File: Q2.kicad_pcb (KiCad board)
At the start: 2 copper layers, 87.7 x 51.6 mm, 145 parts, among them U1 LM317, U10 SP-2U1+, U11 SMA, U12 LT1009, U13 TL974, U2 Teensy3.2, U3 SMA, U4 ROS-2536C-119+, U5 PMA4-33GLN+, U6 PGA-103+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

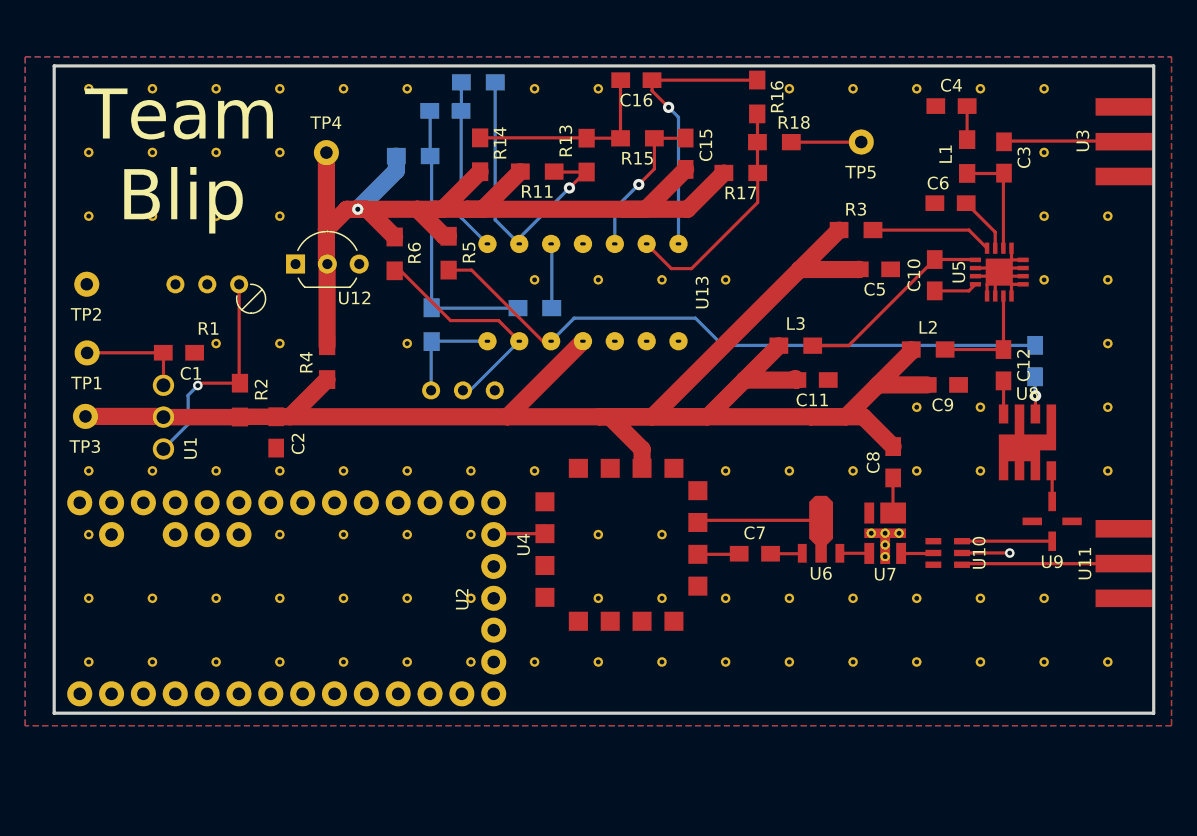
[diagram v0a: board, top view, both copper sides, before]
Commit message: PCB Fix + DFM Report + PCB Width Calculation
Fixed Track Width
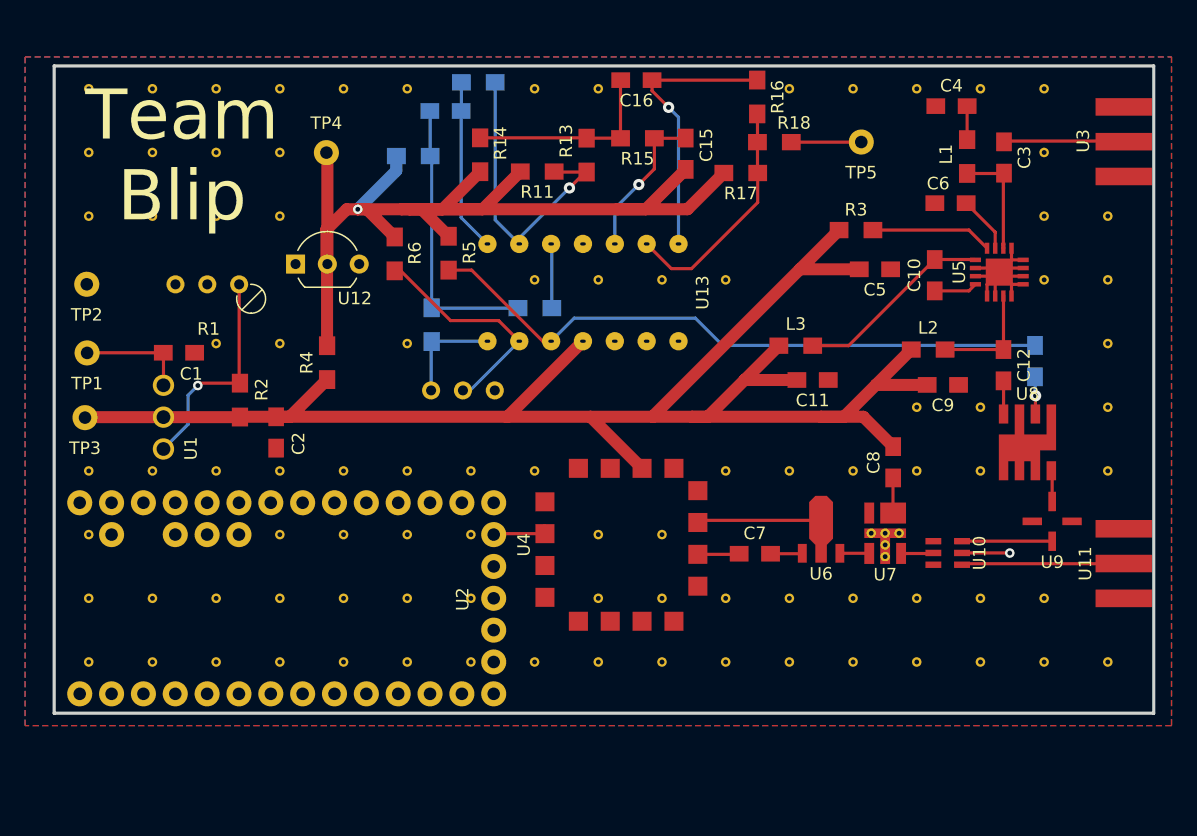
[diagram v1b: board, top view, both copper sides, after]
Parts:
- moved TP3 0.10 mm to (37.8, 59.2)
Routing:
- net /+5V: track 149.9 -> 137.9 mm
- net /+2.5V: track 78.8 -> 87.9 mm

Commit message: Update
Fix Ground Connection Issues
Cleaned Up Ground Connection
Fixed Via Ground Connection Issues
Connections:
- REF** pad 1: (no net) -> GND (x90)
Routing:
- net GND: track 40.6 -> 42.5 mm
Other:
- net class Default: trace_width 0.254 -> 0.508

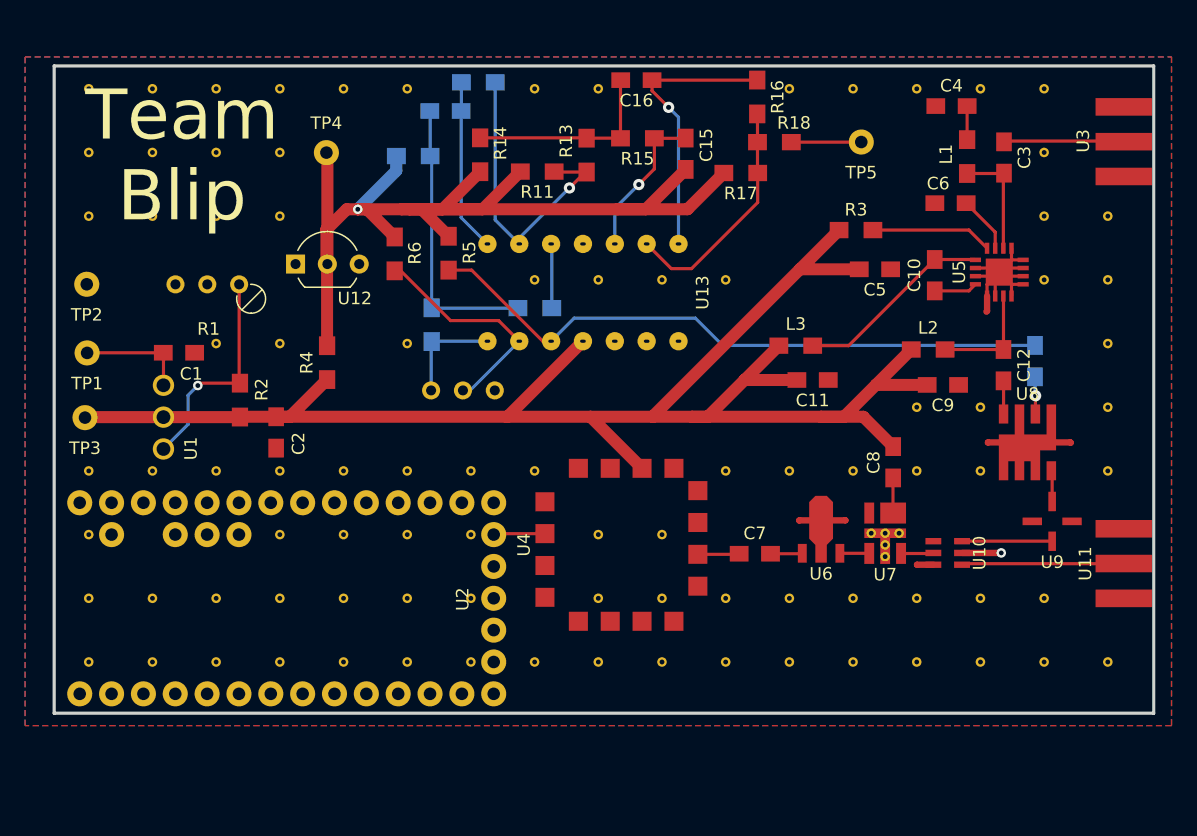
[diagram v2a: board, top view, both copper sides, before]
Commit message: Update
Fixed Missing LNA
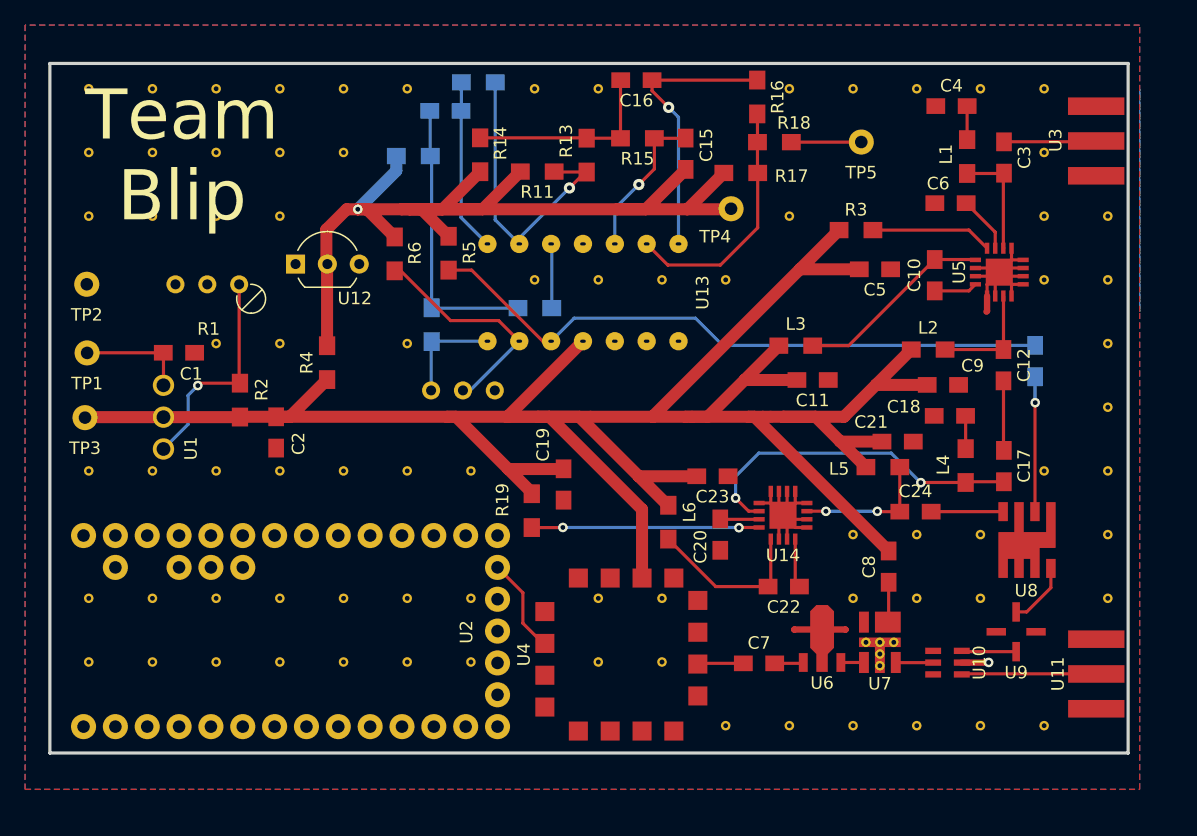
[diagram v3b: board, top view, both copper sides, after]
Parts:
- removed the REF** at (114.3, 73.7)
- removed the REF** at (114.3, 78.7)
- removed the REF** at (119.4, 78.7)
- removed the REF** at (99.1, 78.7)
- removed the REF** at (109.2, 63.5)
- removed the REF** at (109.2, 58.4)
- removed the REF** at (104.1, 63.5)
- removed the REF** at (104.1, 58.4)
- removed the REF** at (99.1, 63.5)
- removed the REF** at (94.0, 63.5)
- removed the REF** at (88.9, 63.5)
- removed the REF** at (88.9, 73.7)
- removed the REF** at (104.1, 78.7)
- removed the REF** at (83.8, 68.6)
- removed the REF** at (78.7, 68.6)
- removed the REF** at (73.7, 78.7)
- removed the REF** at (68.6, 68.6)
- removed the REF** at (63.5, 68.6)
- removed the REF** at (58.4, 68.6)
- removed the REF** at (53.3, 68.6)
- removed the REF** at (94.0, 78.7)
- removed the REF** at (88.9, 78.7)
- removed the REF** at (38.1, 68.6)
- removed the REF** at (73.7, 63.5)
- removed the REF** at (109.2, 78.7)
- removed the REF** at (94.0, 73.7)
- added C17: 56p, Q2Footprint:C_0805_HandSoldering, F.Cu at (111.1, 63.1)
- added C18: 0.1u, Q2Footprint:C_0805_HandSoldering, F.Cu at (106.8, 59.1)
- added C19: 0.1u, Q2Footprint:C_0805_HandSoldering, F.Cu at (76.0, 64.6)
- added C20: 1n, Q2Footprint:C_0805_HandSoldering, F.Cu at (88.5, 68.6)
- added C21: 0.1u, Q2Footprint:C_0805_HandSoldering, F.Cu at (102.6, 61.2)
- added C22: 82p, Q2Footprint:C_0805_HandSoldering, F.Cu at (93.5, 72.7)
- added C23: 0.1u, Q2Footprint:C_0805_HandSoldering, F.Cu at (87.8, 63.9)
- added C24: 0.1u, Q2Footprint:C_0805_HandSoldering, F.Cu at (104.0, 66.8)
- added L4: 15n, Q2Footprint:L_0805_HandSoldering, F.Cu at (108.0, 63.1)
- added L5: 82n, Q2Footprint:L_0805_HandSoldering, F.Cu at (101.4, 63.2)
- added L6: 5.6n, Q2Footprint:L_0805_HandSoldering, F.Cu at (84.3, 67.6)
- added R19: 1k, Q2Footprint:R_0805_HandSoldering, F.Cu at (73.4, 66.7)
- added REF**: via-15mil, Q2Footprint:via-15mil, F.Cu at (58.4, 38.1)
- added REF**: via-15mil, Q2Footprint:via-15mil, F.Cu at (114.3, 63.5)
- added REF**: via-15mil, Q2Footprint:via-15mil, F.Cu at (88.9, 83.8)
- added REF**: via-15mil, Q2Footprint:via-15mil, F.Cu at (94.0, 83.8)
- added REF**: via-15mil, Q2Footprint:via-15mil, F.Cu at (99.1, 83.8)
- added REF**: via-15mil, Q2Footprint:via-15mil, F.Cu at (99.1, 68.6)
- added REF**: via-15mil, Q2Footprint:via-15mil, F.Cu at (104.1, 83.8)
- added REF**: via-15mil, Q2Footprint:via-15mil, F.Cu at (109.2, 83.8)
- added REF**: via-15mil, Q2Footprint:via-15mil, F.Cu at (114.3, 83.8)
- added REF**: via-15mil, Q2Footprint:via-15mil, F.Cu at (119.4, 73.7)
- added REF**: via-15mil, Q2Footprint:via-15mil, F.Cu at (119.4, 68.6)
- added REF**: via-15mil, Q2Footprint:via-15mil, F.Cu at (94.0, 43.2)
- added REF**: via-15mil, Q2Footprint:via-15mil, F.Cu at (109.2, 68.6)
- added REF**: via-15mil, Q2Footprint:via-15mil, F.Cu at (104.1, 68.6)
- added U14: PMA4-33GLN+, Q2Footprint:PMA4-33GLN+, F.Cu at (93.5, 67.0)
- moved TP4 32.6 mm to (89.3, 42.6)
- moved U9 9.26 mm to (112.1, 76.3)
- moved U11 9.07 mm to (116.2, 79.7)
- moved U4 8.75 mm to (80.6, 78.1)
- moved C7 8.75 mm to (91.6, 78.8)
- moved U10 8.75 mm to (106.6, 78.8)
- moved U7 8.71 mm to (101.2, 77.2)
- moved U6 8.71 mm to (96.6, 76.9)
- moved C8 8.33 mm to (101.9, 71.1)
- moved U8 7.79 mm to (112.9, 69.0)
- moved U2 2.63 mm to (72.0, 76.3)
- moved U3 2.20 mm to (120.7, 37.2)
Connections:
- U8 pad 4: Net-(C12-Pad1) -> Net-(C24-Pad1)
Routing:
- net /+5V: track 137.9 -> 203.9 mm
- net Net-(C17-Pad1): track 0.00 -> 27.2 mm, vias 0 -> 2
- net Net-(R19-Pad1): track 0.00 -> 18.2 mm, vias 0 -> 2
- net Net-(C22-Pad1): track 0.00 -> 13.4 mm
- net Net-(C24-Pad2): track 0.00 -> 11.0 mm, vias 0 -> 2
- net Net-(C13-Pad2): track 2.99 -> 10.8 mm
- net GND: track 42.5 -> 50.1 mm
- net Net-(C24-Pad1): track 0.00 -> 5.81 mm
- net /+2.5V: track 87.9 -> 82.3 mm
- net Net-(C22-Pad2): track 0.00 -> 3.92 mm
- net Net-(U2-Pad18): track 4.23 -> 7.71 mm
- net Net-(C20-Pad1): track 0.00 -> 3.11 mm
- net Net-(C12-Pad1): track 2.64 -> 5.58 mm
- net Net-(U10-Pad3): track 7.19 -> 4.36 mm
- net Net-(U8-Pad8): track 2.48 -> 5.11 mm
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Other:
- board size 87.7 x 51.6 mm -> 86 x 55 mm
- net class Default: trace_width 0.508 -> 0.961

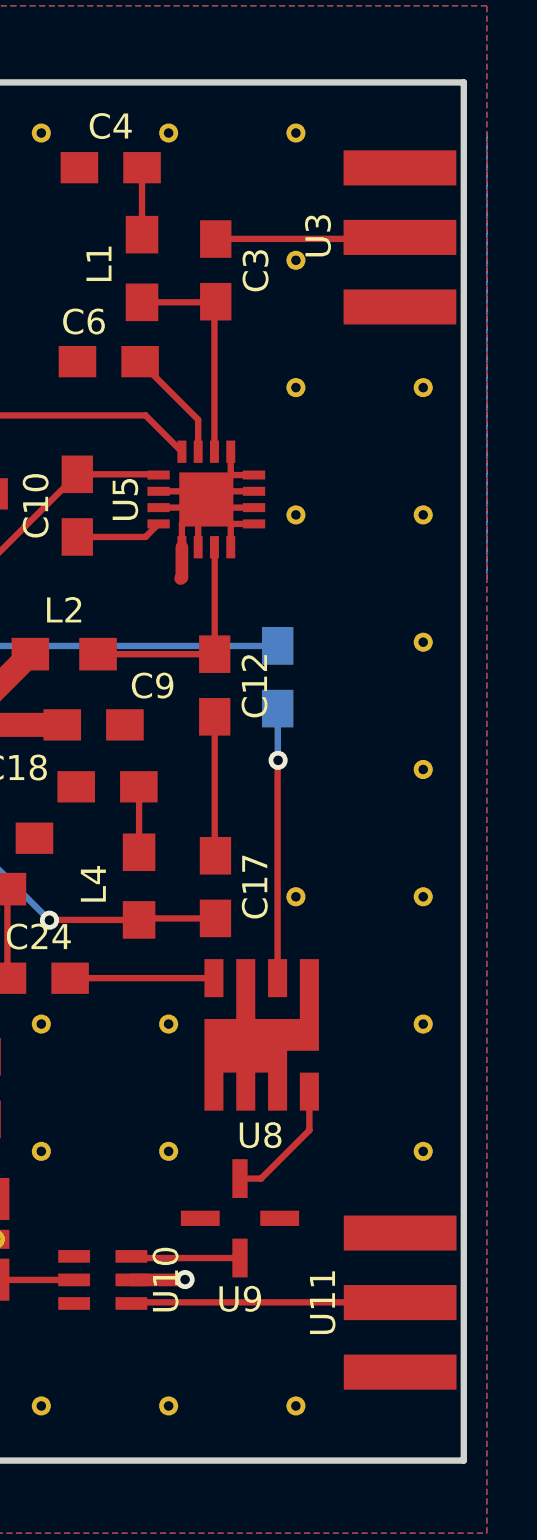
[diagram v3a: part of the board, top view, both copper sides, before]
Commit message: Update
Fixed SMA Edge
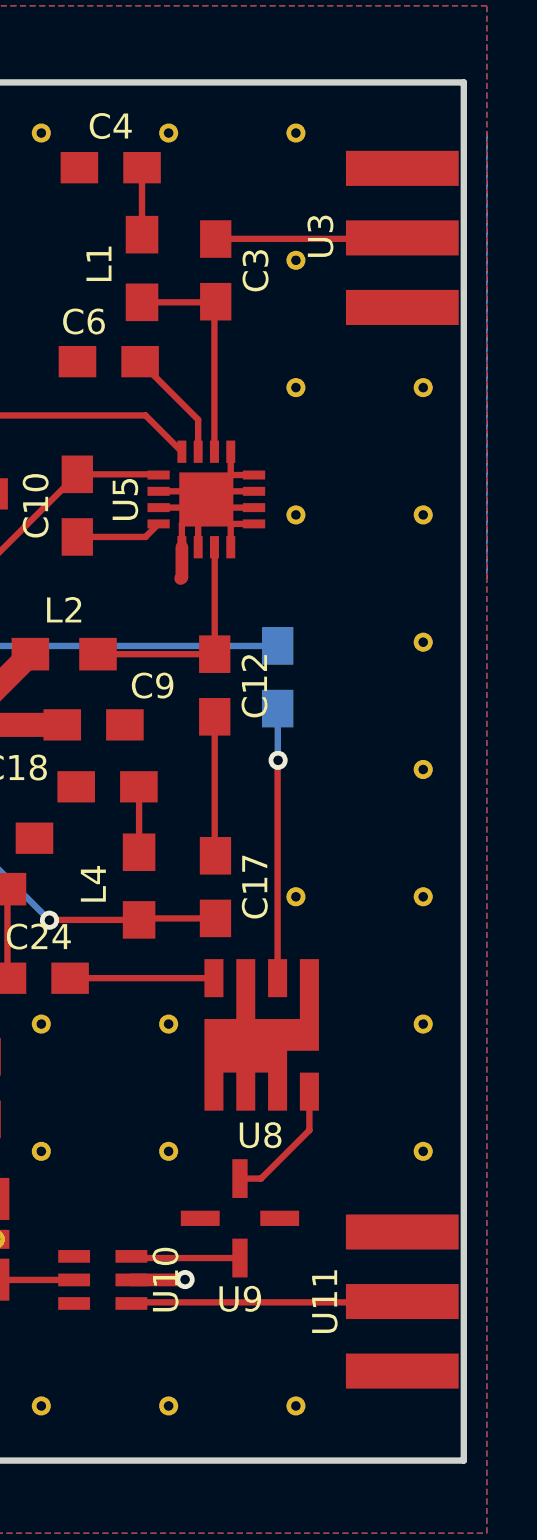
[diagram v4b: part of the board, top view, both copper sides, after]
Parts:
- moved U3 0.10 mm to (120.8, 37.2)
- moved U11 0.10 mm to (116.3, 79.7)
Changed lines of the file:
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@@
   )
   (module Q2Footprint:SMA (layer F.Cu)
-    (at 120.701 37.186 90)
+    (at 120.797 37.206 90)
     (fp_text reference U3 (at 0.061 -5.483 90) (layer F.SilkS)
       (effects (font (size 1 1) (thickness 0.15)))
@@
   )
   (module Q2Footprint:SMA (layer F.Cu)
-    (at 116.21 79.695 270)
+    (at 116.296 79.654 270)
     (fp_text reference U11 (at 0 0.8128 270) (layer F.SilkS)
       (effects (font (size 1 1) (thickness 0.15)))

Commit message: Update
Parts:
- C12, C24: value 0.1u -> 68p
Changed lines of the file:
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@@
     (links 240)
     (no_connects 0)
-    (area 34.872999 30.872999 121.127001 86.127001)
+    (area 33.02 27.94 122.5558 88.900001)
     (thickness 1.6)
     (drawings 5)
@@
       (effects (font (size 1 1) (thickness 0.15)))
     )
-    (fp_text value 0.1u (at 0 -1.524 90) (layer F.Fab)
+    (fp_text value 68p (at 0 -1.524 90) (layer F.Fab)
       (effects (font (size 1 1) (thickness 0.15)))
     )
@@
       (effects (font (size 1 1) (thickness 0.15)))
     )
-    (fp_text value 0.1u (at 0 -1.524 180) (layer F.Fab)
-      (effects (font (size 1 1) (thickness 0.15)))
-    )
+    (fp_text value 68p (at 0 -1.524 180) (layer F.Fab)
+      (effects (font (size 1 1) (thickness 0.15)))
+    )

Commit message: Update
Fixed LNA Connection
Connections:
- C20 pad 1: Net-(C20-Pad1) -> Net-(C18-Pad1)
- C6 pad 1: Net-(C6-Pad1) -> Net-(C4-Pad1)
- U14 pad 3: Net-(C20-Pad1) -> Net-(C18-Pad1)
- U5 pad 3: Net-(C6-Pad1) -> Net-(C4-Pad1)
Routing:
- net Net-(C18-Pad1): track 2.62 -> 31.1 mm, vias 0 -> 2
- net Net-(C4-Pad1): track 2.67 -> 14.3 mm
- net Net-(C6-Pad1): track 4.55 -> 0.00 mm
- net Net-(C20-Pad1): track 3.11 -> 0.00 mm
- net GND: track 50.1 -> 52.0 mm, vias 1 -> 2
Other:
- net class Default: trace_width 0.961 -> 0.508

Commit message: Update
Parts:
- added C25: 1n, Q2Footprint:C_0805_HandSoldering, B.Cu at (73.8, 34.8)
- added REF**: via-15mil, Q2Footprint:via-15mil, F.Cu at (88.9, 38.1)
- added REF**: via-15mil, Q2Footprint:via-15mil, F.Cu at (88.9, 33.0)
- added REF**: via-15mil, Q2Footprint:via-15mil, F.Cu at (94.0, 38.1)
- added REF**: via-15mil, Q2Footprint:via-15mil, F.Cu at (104.1, 43.2)
- added REF**: via-15mil, Q2Footprint:via-15mil, F.Cu at (104.1, 38.1)
- added REF**: via-15mil, Q2Footprint:via-15mil, F.Cu at (99.1, 38.1)
- R13: value 17.4 -> 17.4k
- moved R18 5.70 mm to (95.6, 32.3)
- moved TP5 2.91 mm to (97.0, 36.2)
- turned R16 to 270 degrees
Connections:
- R16 pad 1: Net-(R16-Pad1) -> Net-(C16-Pad2)
- R16 pad 2: Net-(C16-Pad2) -> Net-(R16-Pad2)
- R17 pad 2: Net-(R16-Pad1) -> Net-(R16-Pad2)
- R18 pad 2: Net-(R16-Pad1) -> Net-(C16-Pad2)
- U12 pad 1: Net-(U12-Pad1) -> GND
- U12 pad 3: GND -> Net-(U12-Pad3)
- U13 pad 9: Net-(R16-Pad1) -> Net-(R16-Pad2)
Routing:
- net Net-(R16-Pad2): track 0.00 -> 19.9 mm
- net Net-(R16-Pad1): track 19.9 -> 0.00 mm
- net Net-(C25-Pad2): track 5.14 -> 15.8 mm
- net /+2.5V: track 82.3 -> 87.1 mm, vias 1 -> 2
- net Net-(C16-Pad2): track 22.3 -> 25.2 mm
- net Net-(R18-Pad1): track 5.58 -> 3.88 mm
- net Net-(R10-Pad1): track 24.7 -> 24.1 mm
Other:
- net class Default: trace_width 0.508 -> 0.254
- rule trace_min: 0.254 -> 0.1524

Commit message: Update
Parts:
- added REF**: via-15mil, Q2Footprint:via-15mil, F.Cu at (99.1, 43.2)
- added REF**: via-15mil, Q2Footprint:via-15mil, F.Cu at (58.4, 43.2)
- added REF**: via-15mil, Q2Footprint:via-15mil, F.Cu at (43.2, 53.3)
- added REF**: via-15mil, Q2Footprint:via-15mil, F.Cu at (38.1, 48.3)
- added REF**: via-15mil, Q2Footprint:via-15mil, F.Cu at (88.9, 73.7)
- moved C1 11.6 mm to (45.3, 65.7)
- moved TP1 11.6 mm to (37.7, 65.7)
- moved L3 8.38 mm to (101.1, 48.3)
- moved C5 6.34 mm to (94.5, 48.5)
- moved C11 5.56 mm to (98.1, 51.2)
- moved C9 5.40 mm to (100.9, 57.7)
- moved TP2 4.75 mm to (37.9, 53.4)
- moved C23 4.40 mm to (83.4, 64.0)
- moved C19 3.82 mm to (72.5, 62.9), turned to 0 degrees
- moved C21 3.49 mm to (99.1, 61.0)
- moved L2 2.36 mm to (103.4, 55.5)
- moved R3 2.21 mm to (97.5, 45.6)
- moved R4 2.18 mm to (57.1, 52.7)
- moved U5 1.70 mm to (110.8, 49.3)
- moved C10 1.70 mm to (105.6, 49.6)
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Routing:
- net Net-(C10-Pad1): track 15.8 -> 6.46 mm
- net /+5V: track 203.9 -> 208.9 mm
- net /+2.5V: track 87.1 -> 82.2 mm
- net Net-(R1-Pad1): track 17.5 -> 14.1 mm, vias 1 -> 0
- net Net-(R3-Pad1): track 9.70 -> 11.7 mm
- net GND: track 52.0 -> 50.1 mm, vias 2 -> 1
- net Net-(C3-Pad1): track 9.05 -> 10.8 mm
- net Net-(C12-Pad2): track 8.93 -> 10.6 mm
- net Net-(C12-Pad1): track 5.58 -> 3.94 mm
- net Net-(C1-Pad1): track 8.77 -> 10.2 mm
- net Net-(C4-Pad1): track 14.3 -> 15.4 mm
